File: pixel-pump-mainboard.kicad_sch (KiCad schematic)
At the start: 125 parts, among them J1 JST NC Valve, J10 BM10B-SRSS-TB(LF)(SN), J11 UART/SWD DNP, J12 TYPE-C-31-M-12, J2 JST NO Valve, J3 6P4C, J4 JST 3 Way Valve, J5 Jack-DC 12V, J6 Power Sw, J7 EXP1, J8 EXP2, J9 BM04B-SRSS-TBT(LF)(SN), Q1 BSS138, Q2 BSS138, Q3 BSS138, Q4 STN4NF20L, Q5 BSS138, SW1 BOOTSEL, U1 LD1117S33TR, U2 TPS62112RSAR, U3 W25Q128JVPIQ, U4 RP2040, Y1 ABMM2-12.000MHZ-E2-T

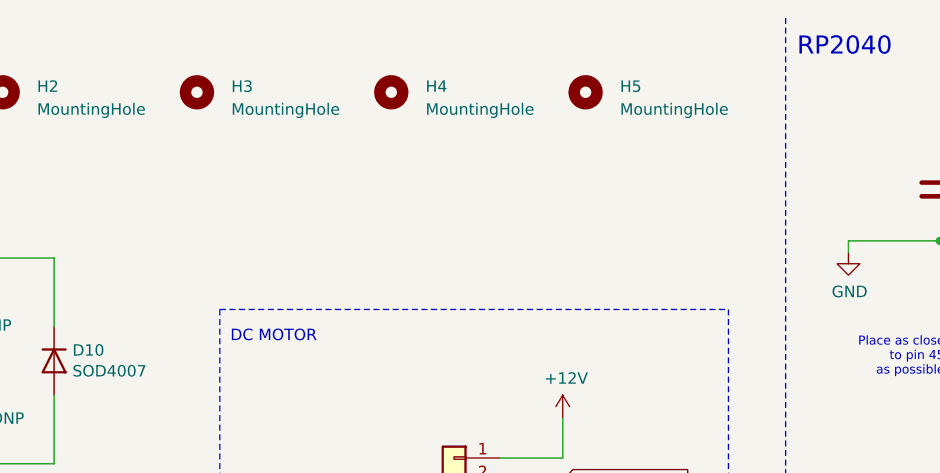
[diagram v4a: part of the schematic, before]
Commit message: Add KiKit annotations
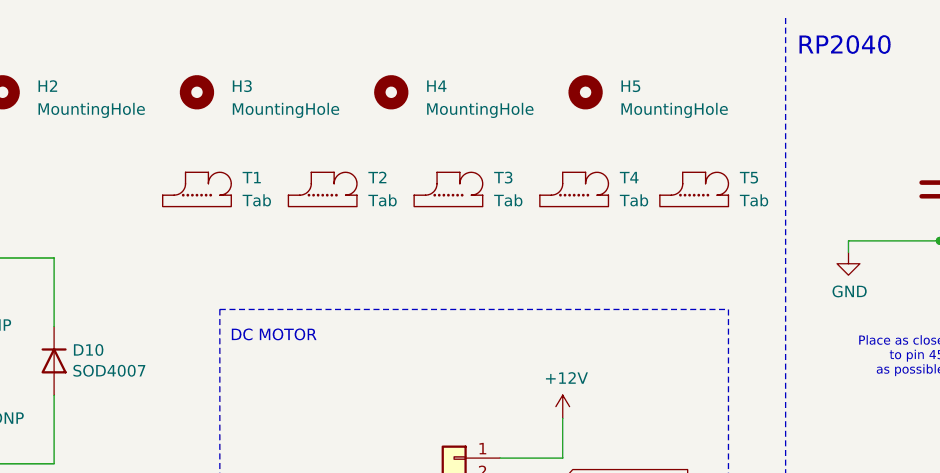
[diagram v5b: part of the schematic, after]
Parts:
- added T1, T2, T3, T4, T5: Tab, kikit:Tab, symbol kikit:Tab
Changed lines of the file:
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@@
     (pin "8")
+  )
+  (symbol (lib_id "kikit:Tab") (at 266.7 32.385 0) (unit 1)
+    (in_bom no) (on_board yes) (fields_autoplaced)
+    (property "Reference" "T5" (id 0) (at 271.78 30.4799 0)
+      (effects (font (size 1.27 1.27)) (justify left))
+    )
+    (property "Value" "Tab" (id 1) (at 271.78 33.0199 0)
+      (effects (font (size 1.27 1.27)) (justify left))
+    )
+    (property "Footprint" "kikit:Tab" (id 2) (at 266.7 32.385 0)
+      (effects (font (size 1.27 1.27)) hide)
+    )
+    (property "Datasheet" "" (id 3) (at 266.7 32.385 0)
+      (effects (font (size 1.27 1.27)) hide)
+    )
   )
   (symbol (lib_id "power:+3V3") (at 333.375 231.14 0) (unit 1)
@@
     )
   )
+  (symbol (lib_id "kikit:Tab") (at 239.395 32.385 0) (unit 1)
+    (in_bom no) (on_board yes) (fields_autoplaced)
+    (property "Reference" "T3" (id 0) (at 244.475 30.4799 0)
+      (effects (font (size 1.27 1.27)) (justify left))
+    )
+    (property "Value" "Tab" (id 1) (at 244.475 33.0199 0)
+      (effects (font (size 1.27 1.27)) (justify left))
+    )
+    (property "Footprint" "kikit:Tab" (id 2) (at 239.395 32.385 0)
+      (effects (font (size 1.27 1.27)) hide)
+    )
+    (property "Datasheet" "" (id 3) (at 239.395 32.385 0)
+      (effects (font (size 1.27 1.27)) hide)
+    )
+  )
   (symbol (lib_id "Device:C") (at 199.39 132.08 0) (unit 1)
     (in_bom yes) (on_board yes) (fields_autoplaced)
@@
     )
     (pin "1")
+  )
+  (symbol (lib_id "kikit:Tab") (at 225.425 32.385 0) (unit 1)
+    (in_bom no) (on_board yes) (fields_autoplaced)
+    (property "Reference" "T2" (id 0) (at 230.505 30.4799 0)
+      (effects (font (size 1.27 1.27)) (justify left))
+    )
+    (property "Value" "Tab" (id 1) (at 230.505 33.0199 0)
+      (effects (font (size 1.27 1.27)) (justify left))
+    )
+    (property "Footprint" "kikit:Tab" (id 2) (at 225.425 32.385 0)
+      (effects (font (size 1.27 1.27)) hide)
+    )
+    (property "Datasheet" "" (id 3) (at 225.425 32.385 0)
+      (effects (font (size 1.27 1.27)) hide)
+    )
   )
   (symbol (lib_id "Device:Polyfuse") (at 53.34 129.54 270) (unit 1)
@@
     (pin "1")
     (pin "2")
+  )
+  (symbol (lib_id "kikit:Tab") (at 253.365 32.385 0) (unit 1)
+    (in_bom no) (on_board yes) (fields_autoplaced)
+    (property "Reference" "T4" (id 0) (at 258.445 30.4799 0)
+      (effects (font (size 1.27 1.27)) (justify left))
+    )
+    (property "Value" "Tab" (id 1) (at 258.445 33.0199 0)
+      (effects (font (size 1.27 1.27)) (justify left))
+    )
+    (property "Footprint" "kikit:Tab" (id 2) (at 253.365 32.385 0)
+      (effects (font (size 1.27 1.27)) hide)
+    )
+    (property "Datasheet" "" (id 3) (at 253.365 32.385 0)
+      (effects (font (size 1.27 1.27)) hide)
+    )
   )
   (symbol (lib_id "power:+5V") (at 143.51 184.15 0) (unit 1)
@@
     (pin "1")
   )
+  (symbol (lib_id "kikit:Tab") (at 211.455 32.385 0) (unit 1)
+    (in_bom no) (on_board yes) (fields_autoplaced)
+    (property "Reference" "T1" (id 0) (at 216.535 30.4799 0)
+      (effects (font (size 1.27 1.27)) (justify left))
+    )
+    (property "Value" "Tab" (id 1) (at 216.535 33.0199 0)
+      (effects (font (size 1.27 1.27)) (justify left))
+    )
+    (property "Footprint" "kikit:Tab" (id 2) (at 211.455 32.385 0)
+      (effects (font (size 1.27 1.27)) hide)
+    )
+    (property "Datasheet" "" (id 3) (at 211.455 32.385 0)
+      (effects (font (size 1.27 1.27)) hide)
+    )
+  )
   (symbol (lib_id "Device:R") (at 254.635 189.23 90) (unit 1)
     (in_bom yes) (on_board yes)
@@
       (reference "SW1") (unit 1) (value "BOOTSEL") (footprint "Button_Switch_THT:SW_Tactile_SKHH_Angled")
     )
+    (path "/eddb214c-a097-4078-8c38-4730f11f51dc"
+      (reference "T1") (unit 1) (value "Tab") (footprint "kikit:Tab")
+    )
+    (path "/5ed76c5f-7263-42e9-ab4a-3a769ec7c995"
+      (reference "T2") (unit 1) (value "Tab") (footprint "kikit:Tab")
+    )
+    (path "/52a0aa46-142e-4c9b-a083-750b3e6809ce"
+      (reference "T3") (unit 1) (value "Tab") (footprint "kikit:Tab")
+    )
+    (path "/84628ad2-8875-4b6c-aedd-9a4631f61f46"
+      (reference "T4") (unit 1) (value "Tab") (footprint "kikit:Tab")
+    )
+    (path "/268a072e-7284-4f19-b28d-76384cd530ca"
+      (reference "T5") (unit 1) (value "Tab") (footprint "kikit:Tab")
+    )
     (path "/00000000-0000-0000-0000-0000615f52e1"

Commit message: Rev 8 panel settings and export
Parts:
- removed T5: Tab, kikit:Tab, symbol kikit:Tab
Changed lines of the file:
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@@
     (pin "8")
-  )
-  (symbol (lib_id "kikit:Tab") (at 266.7 32.385 0) (unit 1)
-    (in_bom no) (on_board yes) (fields_autoplaced)
-    (property "Reference" "T5" (id 0) (at 271.78 30.4799 0)
-      (effects (font (size 1.27 1.27)) (justify left))
-    )
-    (property "Value" "Tab" (id 1) (at 271.78 33.0199 0)
-      (effects (font (size 1.27 1.27)) (justify left))
-    )
-    (property "Footprint" "kikit:Tab" (id 2) (at 266.7 32.385 0)
-      (effects (font (size 1.27 1.27)) hide)
-    )
-    (property "Datasheet" "" (id 3) (at 266.7 32.385 0)
-      (effects (font (size 1.27 1.27)) hide)
-    )
   )
   (symbol (lib_id "power:+3V3") (at 333.375 231.14 0) (unit 1)
@@
       (reference "T4") (unit 1) (value "Tab") (footprint "kikit:Tab")
     )
-    (path "/268a072e-7284-4f19-b28d-76384cd530ca"
-      (reference "T5") (unit 1) (value "Tab") (footprint "kikit:Tab")
-    )
     (path "/00000000-0000-0000-0000-0000615f52e1"

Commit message: Fixed issues and generated the final pos file
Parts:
- J7, J9: footprint Connector_JST:JST_SH_BM04B-SRSS-TB_1x04-1MP_P1.00mm_Vertical -> BM04B-SRSS-TBT:BM04B-SRSS-TBT
- J8: footprint Connector_JST:JST_SH_BM06B-SRSS-TB_1x06-1MP_P1.00mm_Vertical -> BM06B-SRSS-TBT:BM06B-SRSS-TBT
- U1: footprint Package_TO_SOT_SMD:SOT-223-3_TabPin2 -> Package_TO_SOT_SMD:SOT-223
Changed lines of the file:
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@@
     (property "Reference" "U1" (id 0) (at 184.785 171.0182 0))
     (property "Value" "LD1117S33TR" (id 1) (at 184.785 173.3296 0))
-    (property "Footprint" "Package_TO_SOT_SMD:SOT-223-3_TabPin2" (id 2) (at 184.785 172.085 0)
+    (property "Footprint" "Package_TO_SOT_SMD:SOT-223" (id 2) (at 184.785 172.085 0)
       (effects (font (size 1.27 1.27)) hide)
     )
@@
     (property "Reference" "J7" (id 0) (at 367.03 230.505 0))
     (property "Value" "EXP1" (id 1) (at 367.665 233.045 0))
-    (property "Footprint" "Connector_JST:JST_SH_BM04B-SRSS-TB_1x04-1MP_P1.00mm_Vertical" (id 2) (at 363.855 233.68 0)
+    (property "Footprint" "BM04B-SRSS-TBT:BM04B-SRSS-TBT" (id 2) (at 363.855 233.68 0)
       (effects (font (size 1.27 1.27)) hide)
     )
@@
       (effects (font (size 1.27 1.27)) (justify left))
     )
-    (property "Footprint" "Connector_JST:JST_SH_BM06B-SRSS-TB_1x06-1MP_P1.00mm_Vertical" (id 2) (at 398.145 227.965 0)
+    (property "Footprint" "BM06B-SRSS-TBT:BM06B-SRSS-TBT" (id 2) (at 398.145 227.965 0)
       (effects (font (size 1.27 1.27)) hide)
     )
@@
     (property "Reference" "J9" (id 0) (at 240.03 74.295 0))
     (property "Value" "BM04B-SRSS-TBT(LF)(SN)" (id 1) (at 229.235 72.39 0))
-    (property "Footprint" "Connector_JST:JST_SH_BM04B-SRSS-TB_1x04-1MP_P1.00mm_Vertical" (id 2) (at 240.03 64.135 0)
+    (property "Footprint" "BM04B-SRSS-TBT:BM04B-SRSS-TBT" (id 2) (at 240.03 64.135 0)
       (effects (font (size 1.27 1.27)) hide)
     )
@@
     )
     (path "/63c15b5e-c12a-4523-afda-c3d21e50ba5b"
-      (reference "J7") (unit 1) (value "EXP1") (footprint "Connector_JST:JST_SH_BM04B-SRSS-TB_1x04-1MP_P1.00mm_Vertical")
+      (reference "J7") (unit 1) (value "EXP1") (footprint "BM04B-SRSS-TBT:BM04B-SRSS-TBT")
     )
     (path "/ccde1372-9ab3-47ad-9572-4de6238d460d"
-      (reference "J8") (unit 1) (value "EXP2") (footprint "Connector_JST:JST_SH_BM06B-SRSS-TB_1x06-1MP_P1.00mm_Vertical")
+      (reference "J8") (unit 1) (value "EXP2") (footprint "BM06B-SRSS-TBT:BM06B-SRSS-TBT")
     )
     (path "/e5c2696e-219e-4607-9e22-8a199dce175a"
-      (reference "J9") (unit 1) (value "BM04B-SRSS-TBT(LF)(SN)") (footprint "Connector_JST:JST_SH_BM04B-SRSS-TB_1x04-1MP_P1.00mm_Vertical")
+      (reference "J9") (unit 1) (value "BM04B-SRSS-TBT(LF)(SN)") (footprint "BM04B-SRSS-TBT:BM04B-SRSS-TBT")
     )
     (path "/35fdf0b6-a443-403b-a5af-ffb36b6c09ec"
@@
     )
     (path "/00000000-0000-0000-0000-00005fe07207"
-      (reference "U1") (unit 1) (value "LD1117S33TR") (footprint "Package_TO_SOT_SMD:SOT-223-3_TabPin2")
+      (reference "U1") (unit 1) (value "LD1117S33TR") (footprint "Package_TO_SOT_SMD:SOT-223")
     )
     (path "/123b26f0-57ed-4b1d-87b7-6a7a7f162189"
